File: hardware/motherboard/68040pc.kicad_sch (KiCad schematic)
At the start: 10 parts, among them U23 PCF8584, U33 74LVC1G04, X4 ASE-12MHz

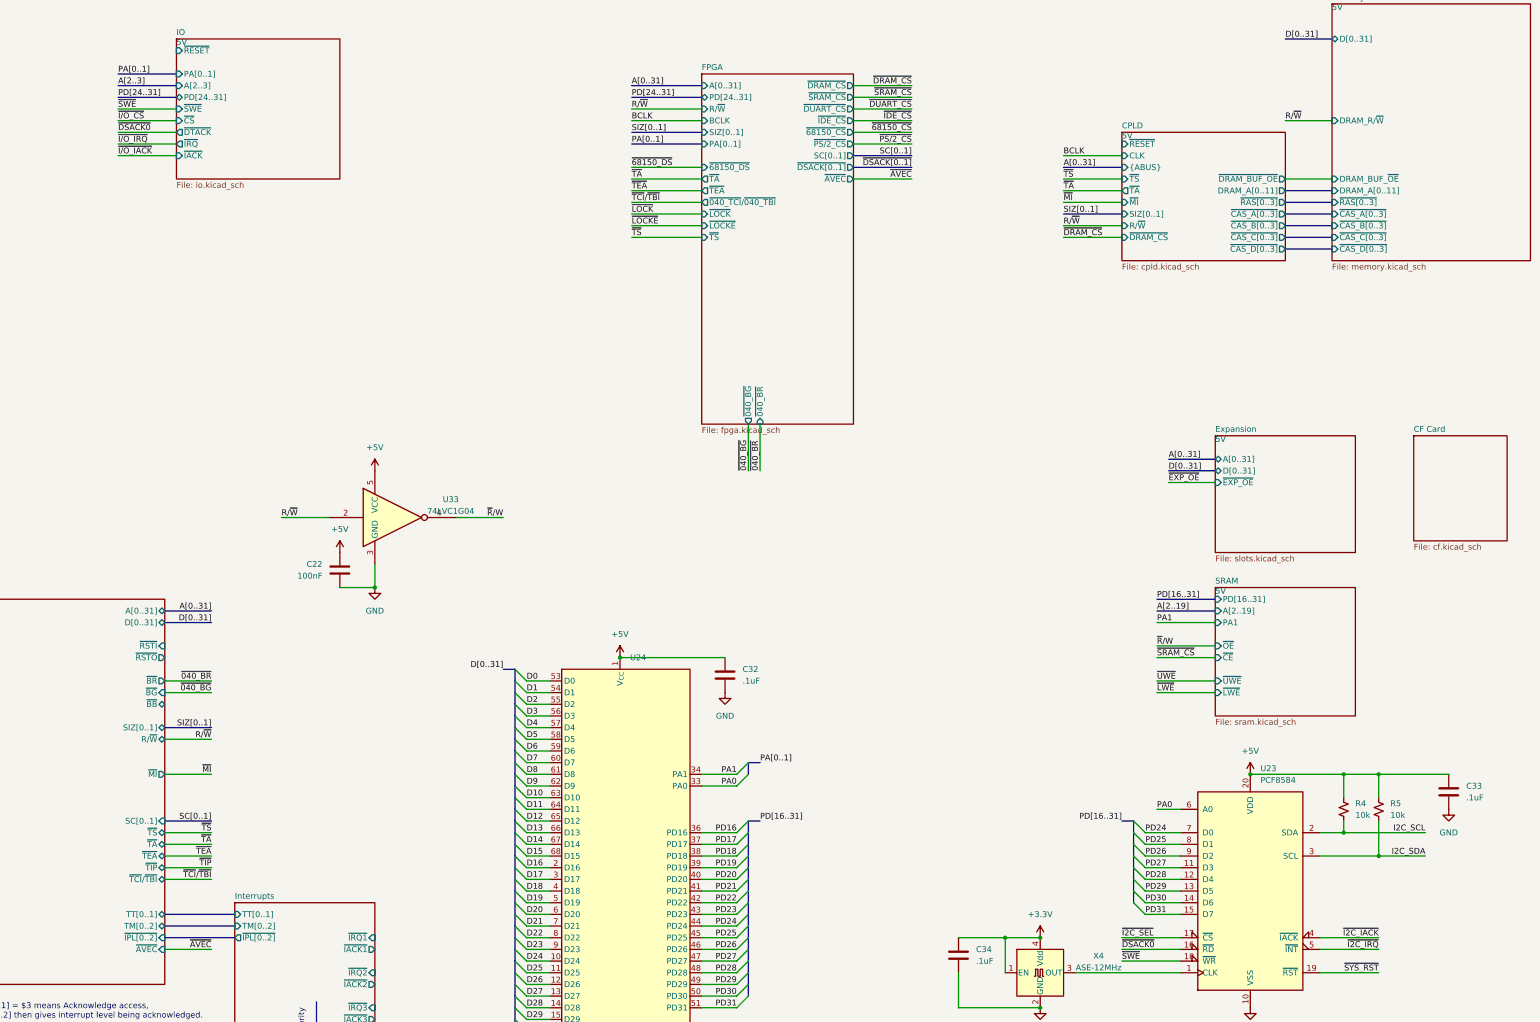
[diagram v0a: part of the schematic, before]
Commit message: restructure, create minimum board project
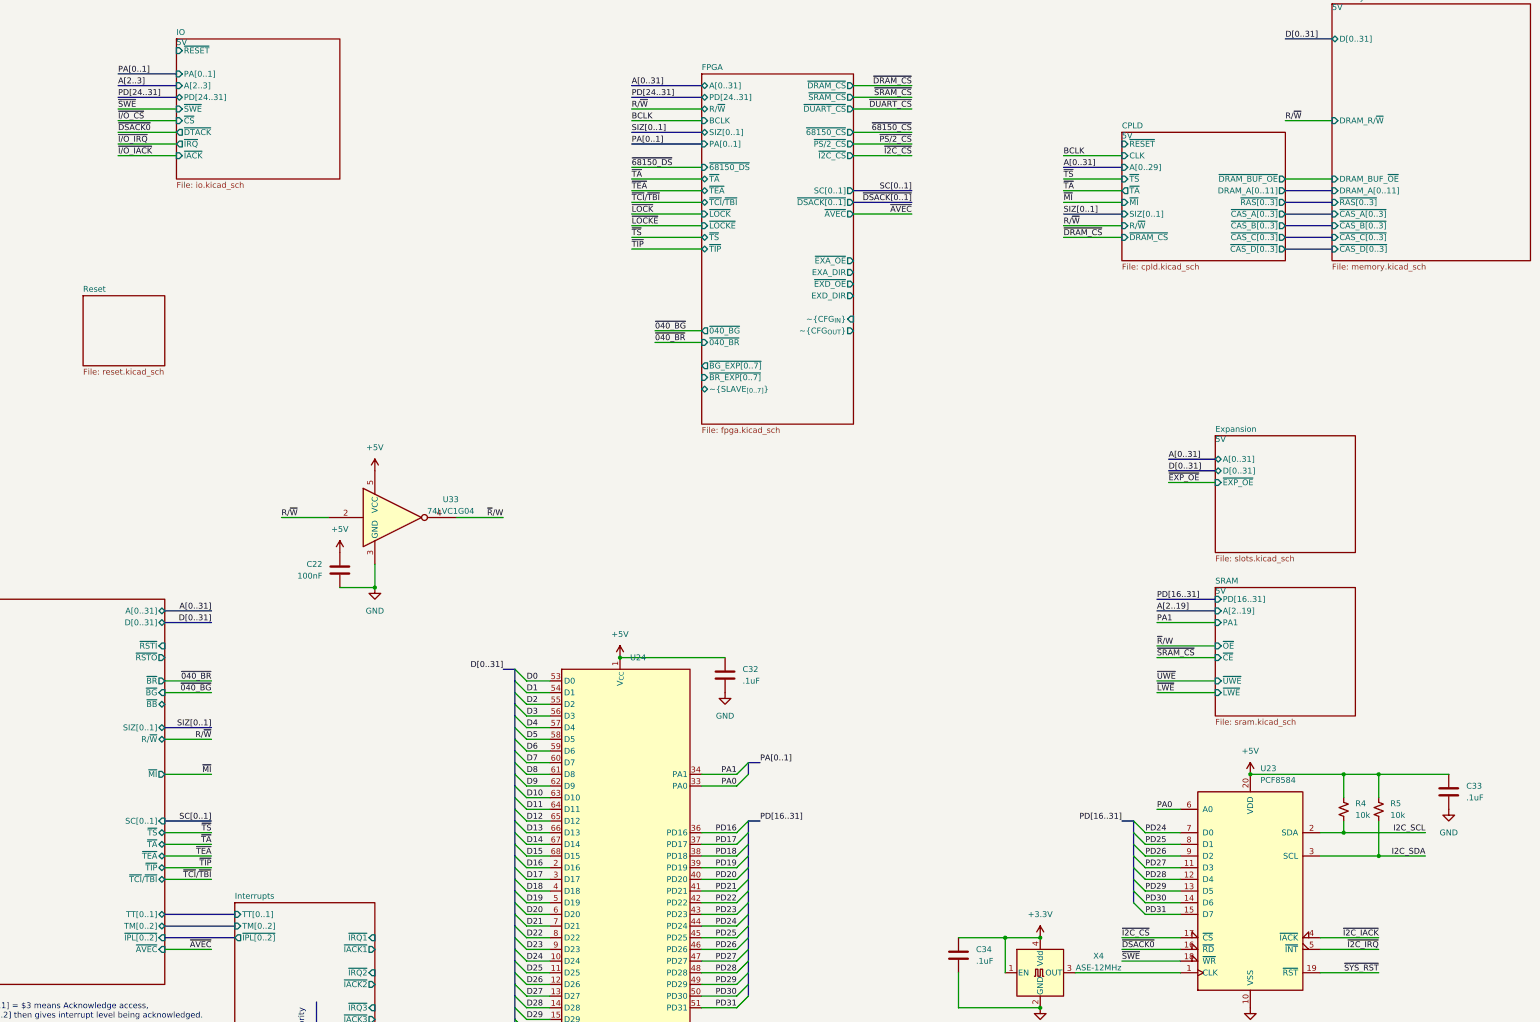
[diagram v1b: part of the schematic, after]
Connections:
- net ~{I2C_SEL} renamed ~{I2C_CS}
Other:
- removed sheet CF Card
- added sheet Reset (reset.kicad_sch)
- sheet CPLD ports: added A[0..29]; removed {ABUS}
- sheet FPGA ports: added EXA_DIR, EXD_DIR, ~{BG_EXP[0..7]}, ~{BR_EXP[0..7]}, ~{CFG_{IN}}, ~{CFG_{OUT}}, ~{EXA_OE}, ~{EXD_OE}, ~{I2C_CS}, ~{SLAVE_{[0..7]}}, ~{TCI}/~{TBI}, ~{TIP}; removed ~{040_TCI}/~{040_TBI}, ~{IDE_CS}

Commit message: work on testboard, move 3d models
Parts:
- renumbered C22 to C56
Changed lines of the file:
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@@
   (symbol (lib_id "Device:C") (at 144.78 138.43 0) (mirror y) (unit 1)
     (in_bom yes) (on_board yes) (dnp no)
-    (property "Reference" "C22" (at 140.97 137.16 0)
+    (property "Reference" "C56" (at 140.97 137.16 0)
       (effects (font (size 1.27 1.27)) (justify left))
     )
@@
     (instances
       (project "68040pc"
-        (path "/3006deba-2100-40f8-9f39-987a5c2c14c7/f9007ce6-1d62-4428-abf8-f7bfb8f1e86d"
-          (reference "C22") (unit 1)
-        )
         (path "/3006deba-2100-40f8-9f39-987a5c2c14c7"
           (reference "C56") (unit 1)
@@
           (reference "#PWR0198") (unit 1)
         )
-        (path "/3006deba-2100-40f8-9f39-987a5c2c14c7/f9007ce6-1d62-4428-abf8-f7bfb8f1e86d"
-          (reference "#PWR099") (unit 1)
-        )
-        (path "/3006deba-2100-40f8-9f39-987a5c2c14c7/fdc28cb7-1567-43bd-b2d6-75893fb1e0c5"
-          (reference "#PWR025") (unit 1)
-        )
       )
     )
@@
           (reference "#PWR0196") (unit 1)
         )
-        (path "/3006deba-2100-40f8-9f39-987a5c2c14c7/f9007ce6-1d62-4428-abf8-f7bfb8f1e86d"
-          (reference "#PWR099") (unit 1)
-        )
-        (path "/3006deba-2100-40f8-9f39-987a5c2c14c7/fdc28cb7-1567-43bd-b2d6-75893fb1e0c5"
-          (reference "#PWR025") (unit 1)
-        )
-      )
+      )
